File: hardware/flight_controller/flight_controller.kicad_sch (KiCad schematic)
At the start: 15 parts, among them U1 BQ25883RGER

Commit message: Finsihed battery charger wiring
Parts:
- added C5: 10uF, symbol Device:C
- added C6: 44uF, symbol Device:C
- added J1: Conn_01x02_Pin, symbol Connector:Conn_01x02_Pin
- added R10: 10K, Resistor_SMD:R_0201_0603Metric, symbol Device:R
- added R11: 30.1K, Resistor_SMD:R_0201_0603Metric, symbol Device:R
- added R8: 383, Resistor_SMD:R_0201_0603Metric, symbol Device:R
- added R9: 5.23K, Resistor_SMD:R_0201_0603Metric, symbol Device:R
- C4: value 4.7uF -> 10uF
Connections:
- net BQ_PG: now also R7.2; no longer R7.1
- net GND: now also C5.1, C6.1, J1.2 (Pin_2), R10.1, R11.1, R8.2
- net VBUS: now also U1.15 (SYS), U1.16 (SYS), C6.2
- net VREGN: now reaches C4.1, U1.11 (REGN)
- net VREGN: now also R9.2
- net BAT+: now reaches U1.13 (BAT)
- net BAT+: now also U1.14 (BAT), C5.2, J1.1 (Pin_1)
- net BQ_CE: now reaches U1.3 (~{CE})
- net at U1.7 (TS): now also R10.2, R11.2, R9.1
- net at U1.8 (ILIM): now also R8.1
- net +3.3V: now reaches R3.1, R4.2, R5.2, R6.2
- net +3.3V: now also R7.1; no longer R7.2
- net BQ_SCL renamed I2C_SCL
- net BQ_SDA renamed I2C_SDA
- no-connect marks 4 -> 5

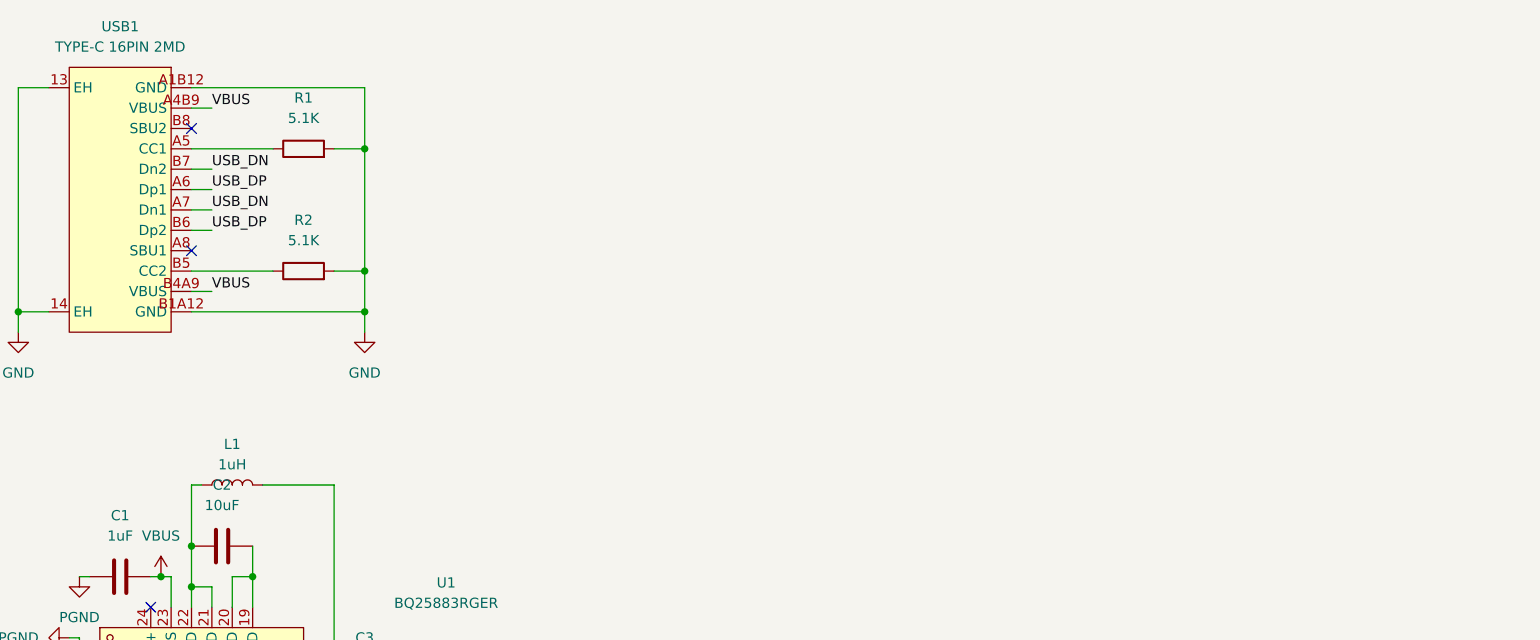
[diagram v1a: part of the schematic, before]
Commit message: Finished wiring for battery regulator
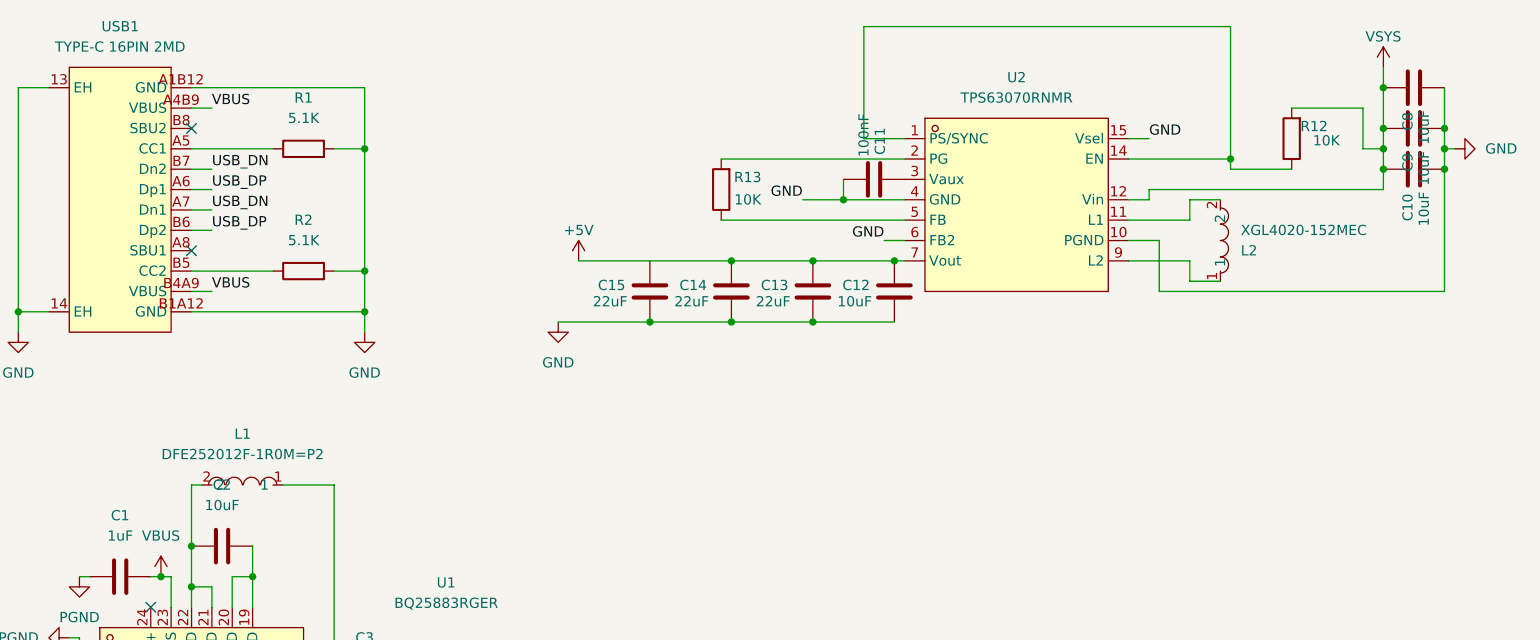
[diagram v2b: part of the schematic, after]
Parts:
- removed L1: 1uH, symbol Device:L
- added C10, C8, C9: 10uF, Capacitor_SMD:C_0805_2012Metric, symbol Device:C
- added C11: 100nF, Capacitor_SMD:C_0805_2012Metric, symbol Device:C
- added C12: 10uF, Capacitor_SMD:C_0603_1608Metric, symbol Device:C
- added C13, C14, C15: 22uF, Capacitor_SMD:C_0805_2012Metric, symbol Device:C
- added L1: DFE252012F-1R0M=P2, easyeda2kicad:L2520, symbol easyeda2kicad:DFE252012F-1R0M=P2
- added L2: XGL4020-152MEC, easyeda2kicad:IND-SMD_L4.0-W4.0_XEL4020, symbol easyeda2kicad:XGL4020-152MEC
- added R12, R13: 10K, Resistor_SMD:R_0201_0603Metric, symbol Device:R
- added U2: TPS63070RNMR, easyeda2kicad:VQFN-15_L3.0-W2.5-P0.50-BL, symbol easyeda2kicad:TPS63070RNMR
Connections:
- net GND: now also C10.2, C11.2, C12.2, C13.2, C14.2, C15.2, C8.2, C9.2, U2.10 (PGND), U2.15 (Vsel), U2.4 (GND), U2.6 (FB2)
- net at C3.1, U1.17 (SW), U1.18 (SW): now also L1.1
- net at C2.1, U1.21 (PMID), U1.22 (PMID): now also L1.2
- new net: R13.1, U2.5 (FB)
- new net: R13.2, U2.2 (PG)
- new net: L2.1, U2.9 (L2)
- new net: L2.2, U2.11 (L1)
- new net: R12.1, U2.1 (PS/SYNC), U2.14 (EN)
- new net: C11.1, U2.3 (Vaux)
- new net +5V: C12.1, C13.1, C14.1, U2.7 (Vout)
- new net VSYS: C10.1, C8.1, C9.1, R12.2, U2.12 (Vin)

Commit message: Wired 3.3V buck, barometer, and IMU
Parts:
- added C15: 2.2uF, Capacitor_SMD:C_0603_1608Metric, symbol Device:C
- added C16, C19, C20, C21, C22: 100nF, Capacitor_SMD:C_0201_0603Metric, symbol Device:C
- added C17, C18: 22uF, Capacitor_SMD:C_0402_1005Metric, symbol Device:C
- added L3: YHNR3015-5R6M, easyeda2kicad:IND-SMD_L3.0-W3.0, symbol easyeda2kicad:YHNR3015-5R6M
- added R14: 100K, Resistor_SMD:R_0402_1005Metric, symbol Device:R
- added R15: 22.1K, Resistor_SMD:R_0402_1005Metric, symbol Device:R
- added U3: LMR51430XDDCR, easyeda2kicad:SOT-23-6_L2.9-W1.6-P0.95-LS2.8-BL, symbol easyeda2kicad:LMR51430XDDCR
- added U4: BMP581, easyeda2kicad:LGA-10_L2.0-W2.0-P0.50-TL_BMP581, symbol easyeda2kicad:BMP581
- added U5: ICM-45686, easyeda2kicad:LGA-14_L3.0-W2.5-P0.50-TL, symbol easyeda2kicad:ICM-45686
- renumbered C11 to C10, C12 to C11, C13 to C12, C14 to C13, C15 to C14, C8 to C7, C9 to C8, C10 to C9
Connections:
- net +3.3V: now also C17.1, C18.1, C19.1, C20.1, C21.1, C22.1, L3.2, R14.2, U4.1 (VDDIO), U4.10 (VDD), U4.6 (CSB), U5.5 (VDDIO), U5.8 (VDD)
- net GND: now also C15.2, C17.2, C18.2, C19.2, C20.2, C21.2, C22.2, R15.1, U3.1 (GND), U4.3 (VSS), U4.5 (SDO), U4.8 (VSS), U4.9 (VSS), U5.6 (GND)
- net I2C_SCL: now also U4.2 (SCK)
- net I2C_SDA: now also U4.4 (SDI)
- net VSYS: now also C15.1, U3.3 (VIN), U3.5 (EN)
- new net: C16.2, L3.1, U3.2 (SW)
- new net: R14.1, R15.2, U3.4 (FB)
- new net: C16.1, U3.6 (CB)
- new net BMP_INT: U4.7 (INT)
- new net ICM_CS: U5.12 (AP_CS)
- new net ICM_INT1: U5.4 (INT1/INT)
- new net ICM_INT2: U5.9 (INT2/FSYNC/CLKIN)
- new net ICM_SCK: U5.13 (AP_SCL/AP_SCLK)
- new net ICM_SDI: U5.14 (AP_SDA/AP_SDIO/AP_SDI)
- new net ICM_SDO: U5.1 (AP_SDO/AP_AD0)
- no-connect marks 5 -> 10

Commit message: GPS, MicroSD, and Magnetometer
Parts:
- added C23: 220nF, Capacitor_SMD:C_0201_0603Metric, symbol Device:C
- added C24, C26: 100nF, Capacitor_SMD:C_0201_0603Metric, symbol Device:C
- added C25: 10uF, Capacitor_SMD:C_0201_0603Metric, symbol Device:C
- added C27: 47pF, Capacitor_SMD:C_0201_0603Metric, symbol Device:C
- added Card1: TF-01A, easyeda2kicad:TF-SMD_TF-01A, symbol easyeda2kicad:TF-01A
- added JP1: U.FL-R-SMT-1, easyeda2kicad:ANT-SMD_UFL-R-SMT-1-10, symbol easyeda2kicad:U.FL-R-SMT-1
- added L4: LQG15HN27NJ02D, easyeda2kicad:L0402, symbol easyeda2kicad:LQG15HN27NJ02D
- added R16, R17, R18, R19, R20, R21: 10K, Resistor_SMD:R_0201_0603Metric, symbol Device:R
- added R22: 120, Resistor_SMD:R_0201_0603Metric, symbol Device:R
- added R23: 10, Resistor_SMD:R_0201_0603Metric, symbol Device:R
- added TP2: TestPoint, symbol Connector:TestPoint
- added U6: LIS2MDLTR, easyeda2kicad:VLGA-12_L2.0-W2.0-P0.50-BL, symbol easyeda2kicad:LIS2MDLTR
- added U7: NEO-M8U-06B, easyeda2kicad:GPSM-SMD_24P-L16.0-W12.2-P1.10-TL, symbol easyeda2kicad:NEO-M8U-06B
- added U8: YLED0603G, easyeda2kicad:LED0603-FD, symbol easyeda2kicad:YLED0603G
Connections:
- net +3.3V: now also C24.1, C25.1, C26.1, Card1.4 (VDD), R16.2, R17.2, R18.2, R19.2, R20.2, R21.2, U6.10 (Vdd_IO), U6.9 (Vdd), U7.22 (V_BCKP), U7.23 (VCC)
- net +5V: now also C14.1
- net GND: now also C2.2, U1.19 (GND), U1.20 (GND), C23.2, C24.2, C25.2, C26.2, C27.2, Card1.10 (GND), Card1.11 (GND), Card1.12 (GND), Card1.13 (GND), Card1.6 (VSS), JP1.1 (GND), JP1.3 (GND), U6.6 (GND), U6.8 (GND), U7.10 (GND), U7.12 (GND), U7.13 (GND), U7.2 (D_SEL), U7.24 (GND), U7.7 (VDD_USB), U8.2 (-)
- new net: C23.1, U6.5 (C1)
- new net: R22.1, U8.1 (+)
- new net: R22.2, U7.3 (TIMEPULSE)
- new net: C27.1, L4.2, R23.1
- new net: R23.2, U7.9 (VCC_RF)
- new net: TP2.1, U7.1 (SAFEBOOT_N)
- new net GPS_CS: U7.18 (SDA/SPICS_N)
- new net GPS_EXTINT: U7.4 (EXTINT)
- new net GPS_RESETN: U7.8 (RESET_N)
- new net GPS_SCK: U7.19 (SCL/SPICLK)
- new net GPS_SDI: U7.21 (RXD/SPIMOSI)
- new net GPS_SDO: U7.20 (TXD/SPIMISO)
- new net MAG_CS: U6.3 (CS)
- new net MAG_SCK: U6.1 (SCL/SPC)
- new net MAG_SDI: U6.4 (SDA/SDI/SDO)
- new net MAG_SDO: U6.7 (INT/DRDY/SDO)
- new net RF_IN: JP1.2 (SIN), L4.1, U7.11 (RF_IN)
- new net SD_CD: Card1.9 (CD)
- new net SD_CLK: Card1.5 (CLK(SCLK)), R21.1
- new net SD_CMD: Card1.3 (CMD(DI)), R20.1
- new net SD_DAT0: Card1.7 (DAT0(D0)), R16.1
- new net SD_DAT1: Card1.8 (DAT1(RSV)), R17.1
- new net SD_DAT2: Card1.1 (DAT2(RSV)), R18.1
- new net SD_DAT3: Card1.2 (CDDAT3(CS)), R19.1
- no-connect marks 10 -> 19
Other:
- moved on the sheet: C1, C10, C11, C12, C13, C14, C15, C16, C17, C18, C19, C2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

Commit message: nothing
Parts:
- added C28: 100nF, Capacitor_SMD:C_0201_0603Metric, symbol Device:C
- added U9: Ai-Thinker-Ra-02, RF_Module:Ai-Thinker-Ra-01-LoRa, symbol RF_Module:Ai-Thinker-Ra-02
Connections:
- net +3.3V: now also C28.1, U9.3 (VDD)
- net GND: now also C28.2, U9.1 (GND), U9.16 (GND), U9.2 (GND), U9.9 (GND)
- net VBUS: no longer C6.2, U1.15 (SYS), U1.16 (SYS)
- net VSYS: now also C6.2, U1.15 (SYS), U1.16 (SYS)
- net GPS_RESETN renamed GPS_RESET
- new net RF_CS: U9.15 (~{NSS})
- new net RF_DIO0: U9.5 (DIO0)
- new net RF_DIO1: U9.6 (DIO1)
- new net RF_DIO2: U9.7 (DIO2)
- new net RF_DIO3: U9.8 (DIO3)
- new net RF_DIO4: U9.10 (DIO4)
- new net RF_DIO5: U9.11 (DIO5)
- new net RF_RESET: U9.4 (~{RESET})
- new net RF_SCK: U9.12 (SCK)
- new net RF_SDI: U9.14 (MOSI)
- new net RF_SDO: U9.13 (MISO)

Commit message: Finsihed schematic
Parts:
- removed C1: 1uF, symbol Device:C
- removed C2, C4, C5: 10uF, symbol Device:C
- removed C3: 47nF, symbol Device:C
- removed C6: 44uF, symbol Device:C
- removed D1: LED, symbol Device:LED
- removed J1: Conn_01x02_Pin, symbol Connector:Conn_01x02_Pin
- removed L1: DFE252012F-1R0M=P2, easyeda2kicad:L2520, symbol easyeda2kicad:DFE252012F-1R0M=P2
- removed R10: 10K, Resistor_SMD:R_0201_0603Metric, symbol Device:R
- removed R11: 30.1K, Resistor_SMD:R_0201_0603Metric, symbol Device:R
- removed R3, R4, R5, R6, R7: 10K, symbol Device:R
- removed R8: 383, Resistor_SMD:R_0201_0603Metric, symbol Device:R
- removed R9: 5.23K, Resistor_SMD:R_0201_0603Metric, symbol Device:R
- removed U1: BQ25883RGER, easyeda2kicad:VFQFPN-24_L4.0-W4.0-P0.50-BL-EP2.8, symbol easyeda2kicad:BQ25883RGER
- added C29, C30, C31, C32, C33, C42, C45: 100nF, Capacitor_SMD:C_0201_0603Metric, symbol Device:C
- added C34, C35, C36, C46, C47: 1uF, Capacitor_SMD:C_0402_1005Metric, symbol Device:C
- added C37: 10uF, Capacitor_SMD:C_0402_1005Metric, symbol Device:C
- added C38, C39: 20pF, Capacitor_SMD:C_0201_0603Metric, symbol Device:C
- added C40, C41: 6.8pF, Capacitor_SMD:C_0201_0603Metric, symbol Device:C
- added C43, C44: 2.2uF, Capacitor_SMD:C_0603_1608Metric, symbol Device:C
- added C48, C50: 10uF, Capacitor_SMD:C_0603_1608Metric, symbol Device:C
- added C49: 4.7uF, Capacitor_SMD:C_0402_1005Metric, symbol Device:C
- added C51: 47nF, Capacitor_SMD:C_0201_0603Metric, symbol Device:C
- added D2: LED, easyeda2kicad:LED0603-FD, symbol Device:LED
- added J2: Camera_Connector, symbol Connector_Generic:Conn_01x06
- added J3: ESC_Connector, symbol Connector_Generic:Conn_01x08
- added J4: ESC_Battery_Solder_Pads, Library:ESC_BATTERY_SOLDER_PADS, symbol Connector_Generic:Conn_01x02
- added J5: Battery_Connector, Connector_JST:JST_XH_B3B-XH-A_1x03_P2.50mm_Vertical, symbol Connector_Generic:Conn_01x03
- added JP2: U.FL-R-SMT-1, easyeda2kicad:ANT-SMD_UFL-R-SMT-1-10, symbol easyeda2kicad:U.FL-R-SMT-1
- added L5: FCM1608KF-601T03, easyeda2kicad:L0603, symbol easyeda2kicad:FCM1608KF-601T03
- added L6: DFE252012F-1R0M=P2, easyeda2kicad:L2520, symbol easyeda2kicad:DFE252012F-1R0M=P2
- added R24, R35: 10K, Resistor_SMD:R_0201_0603Metric, symbol Device:R
- added R25, R26, R27, R28, R29: 10K, symbol Device:R
- added R30: 383, Resistor_SMD:R_0201_0603Metric, symbol Device:R
- added R31: 300, Resistor_SMD:R_0201_0603Metric, symbol Device:R
- added R32: 15, Resistor_SMD:R_1206_3216Metric, symbol Device:R
- added R33: 5.23K, Resistor_SMD:R_0201_0603Metric, symbol Device:R
- added R34: 30.1K, Resistor_SMD:R_0201_0603Metric, symbol Device:R
- added SW1, SW2: TS-1088-AR02016, easyeda2kicad:SW-SMD_L3.9-W3.0-P4.45, symbol easyeda2kicad:TS-1088-AR02016
- added U10: STM32H743VIT6_C114409, easyeda2kicad:LQFP-100_L14.0-W14.0-P0.50-LS16.0-BL, symbol easyeda2kicad:STM32H743VIT6_C114409
- added U11: ANT1204F002R0433A, footprints:CHIP_R0433A_YAG, symbol PassiveAntennaSMDForLoRa:ANT1204F002R0433A
- added U12: BQ25887RGER, easyeda2kicad:WQFN-24_EP_4.0X4.0X0.5P, symbol easyeda2kicad:BQ25887RGER
- added X1: X322525MOB4SI, easyeda2kicad:CRYSTAL-SMD_4P-L3.2-W2.5-BL, symbol easyeda2kicad:X322525MOB4SI
- added X2: Q13FC1350000400, easyeda2kicad:FC-135R_L3.2-W1.5, symbol easyeda2kicad:Q13FC1350000400
- C10: footprint Capacitor_SMD:C_0805_2012Metric -> Capacitor_SMD:C_0201_0603Metric
- C25: footprint Capacitor_SMD:C_0201_0603Metric -> Capacitor_SMD:C_0402_1005Metric
- C9: footprint Capacitor_SMD:C_0805_2012Metric -> Capacitor_SMD:C_0603_1608Metric
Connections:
- net ICM_SCK is gone; now on net SPI_SCK: U5.13 (AP_SCL/AP_SCLK)
- net ICM_SDI is gone; now on net SPI_SDI: U5.14 (AP_SDA/AP_SDIO/AP_SDI)
- net ICM_SDO is gone; now on net SPI_SDO: U5.1 (AP_SDO/AP_AD0)
- net MAG_SCK is gone; now on net SPI_SCK: U6.1 (SCL/SPC)
- net MAG_SDI is gone; now on net SPI_SDI: U6.4 (SDA/SDI/SDO)
- net MAG_SDO is gone; now on net SPI_SDO: U6.7 (INT/DRDY/SDO)
- net RF_SCK is gone; now on net SPI_SCK: U9.12 (SCK)
- net RF_SDI is gone; now on net SPI_SDI: U9.14 (MOSI)
- net RF_SDO is gone; now on net SPI_SDO: U9.13 (MISO)
- net +3.3V: now also C29.1, C30.1, C31.1, C32.1, C33.1, C34.1, C35.1, C36.1, C37.1, C45.1, C46.1, D2.1 (K), L5.2, R25.2, R26.2, R28.2, R29.2, SW2.1, U10.100 (VDD), U10.11 (VDD), U10.27 (VDD), U10.50 (VDD), U10.6 (VBAT), U10.75 (VDD)
- net +5V: now also R13.1, U2.5 (FB), J2.1 (Pin_1)
- net BMP_INT: now also U10.59 (PD12)
- net BQ_CE: now also U10.58 (PD11), U12.3 (CD)
- net BQ_INT: now also R28.1, U10.60 (PD13), U12.6 (~{INT})
- net BQ_PG: now also R29.1, U12.1 (~{PG})
- net GND: now also C29.2, C30.2, C31.2, C32.2, C33.2, C34.2, C35.2, C36.2, C37.2, C38.2, C39.2, C40.2, C41.2, C42.1, C43.2, C44.2, C45.2, C46.2, C47.1, C48.1, C49.2, C50.1, J2.2 (Pin_2), J2.5 (Pin_5), J3.2 (Pin_2), J4.2 (Pin_2), J5.1 (Pin_1), JP2.1 (GND), JP2.3 (GND), R24.1, R30.2, R34.1, R35.1, SW1.1, U10.10 (VSS), U10.19 (VSSA), U10.26 (VSS), U10.49 (VSS), U10.74 (VSS), U10.99 (VSS), U12.19 (GND), U12.20 (GND), U12.24 (PSEL), U12.25 (EP), X1.2 (GND), X1.4 (GND)
- net GPS_CS: now also U10.35 (PB1)
- net GPS_EXTINT: now also U10.25 (PA3)
- net GPS_RESET: now also U10.24 (PA2)
- net I2C_SCL: now also R26.1, U10.92 (PB6), U12.5 (SCL)
- net I2C_SDA: now also R25.1, U10.93 (PB7), U12.4 (SDA)
- net ICM_CS: now also U10.28 (PA4)
- net ICM_INT1: now also U10.32 (PC4)
- net ICM_INT2: now also U10.33 (PC5)
- net MAG_CS: now also U10.34 (PB0)
- net RF_CS: now also U10.36 (PB2)
- net RF_DIO0: now also U10.23 (PA1)
- net RF_DIO1: now also U10.1 (PE2)
- net RF_RESET: now also U10.22 (PA0)
- net SD_CD: now also U10.81 (PD0)
- net SD_CLK: now also U10.80 (PC12)
- net SD_CMD: now also U10.83 (PD2)
- net SD_DAT0: now also U10.65 (PC8)
- net SD_DAT1: now also U10.66 (PC9)
- net SD_DAT2: now also U10.78 (PC10)
- net SD_DAT3: now also U10.79 (PC11)
- net USB_DN: now also U10.70 (PA11)
- net VBUS: now also C47.2, U12.23 (VBUS)
- net VREGN: now also C48.2, R33.2, U12.11 (REGN)
- net at USB1.A6 (Dp1), USB1.B6 (Dp2): now also U10.71 (PA12)
- net GPS_SCK renamed SPI_SCK
- net SPI_SCK: now also U10.29 (PA5)
- net GPS_SDI renamed SPI_SDI
- net SPI_SDI: now also U10.31 (PA7)
- net GPS_SDO renamed SPI_SDO
- net SPI_SDO: now also U10.30 (PA6)
- net RF_DIO2: no longer names the net of U9.7 (DIO2)
- net RF_DIO3: no longer names the net of U9.8 (DIO3)
- net RF_DIO4: no longer names the net of U9.10 (DIO4)
- net RF_DIO5: no longer names the net of U9.11 (DIO5)
- new net: R27.1, U12.2 (STAT)
- new net: D2.2 (A), R27.2
- new net: C43.1, U10.73 (VCAP)
- new net: R32.1, U12.10 (CBSET)
- new net: C51.1, U12.12 (BTST)
- new net: J5.3 (Pin_3), U12.13 (BAT), U12.14 (BAT)
- new net: C49.1, U12.15 (SNS), U12.16 (SNS)
- new net: C51.2, L6.1, U12.17 (SW), U12.18 (SW)
- new net: C50.2, L6.2, U12.21 (PMID), U12.22 (PMID)
- new net: R33.1, R34.2, R35.2, U12.7 (TS)
- new net: R30.1, U12.8 (ILIM)
- new net: R31.1, U12.9 (MID)
- new net: L5.1, U10.20 (VREF+), U10.21 (VDDA)
- new net: C44.1, U10.48 (VCAP)
- new net: J5.2 (Pin_2), R31.2, R32.2
- new net ANT_IN: JP2.2 (SIN), U11.1
- new net BAT_POSITIVE: J4.1 (Pin_1)
- new net BOOT: R24.2, SW2.2, U10.94 (BOOT0)
- new net CAM_RX: J2.3 (Pin_3), U10.98 (PE1)
- new net CAM_TX: J2.4 (Pin_4), U10.97 (PE0)
- new net ESC_BAT: J3.1 (Pin_1), U10.16 (PC1)
- new net ESC_M1: J3.3 (Pin_3), U10.39 (PE9)
- new net ESC_M2: J3.4 (Pin_4), U10.41 (PE11)
- new net ESC_M3: J3.5 (Pin_5), U10.43 (PE13)
- new net ESC_M4: J3.6 (Pin_6), U10.44 (PE14)
- new net HSE_IN: C38.1, U10.12 (PH0-OSC_IN), X1.1 (OSC1)
- new net HSE_OUT: C39.1, U10.13 (PH1-OSC_OUT), X1.3 (OSC2)
- new net LSE_IN: C40.1, U10.8 (PC14-OSC32_IN), X2.1
- new net LSE_OUT: C41.1, U10.9 (PC15-OSC32_OUT), X2.2
- new net RESET: C42.2, SW1.2, U10.14 (NRST)
- no-connect marks 19 -> 66
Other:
- note added: "3.3V Buck"
- note added: "5V Buck Boost"
- note added: "Antenna"
- note added: "Barometer"
- note added: "Battery Charger"
- note added: "Connectors"
- note added: "Crystals"
- note added: "GPS"
- note added: "IMU"
- note added: "LoRa Transmitter"
- note added: "Magnetometer"
- note added: "MicroSD"
- note added: "Microcontroller"
- note added: "Switches"
- note added: "USB"
- title: (none) -> Express Flight Controller
- moved on the sheet: C10, C11, C12, C13, C14, C15, C16, C17, C18, C19, C20, C21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

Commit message: PCB Deisgn Part 1
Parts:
- removed J4: ESC_Battery_Solder_Pads, Library:ESC_BATTERY_SOLDER_PADS, symbol Connector_Generic:Conn_01x02
- added C52: 10uF, Capacitor_SMD:C_0603_1608Metric, symbol Device:C
- C43, C44: footprint Capacitor_SMD:C_0603_1608Metric -> Capacitor_SMD:C_0201_0603Metric
- C48, C50: footprint Capacitor_SMD:C_0603_1608Metric -> Capacitor_SMD:C_0402_1005Metric
- D2: footprint easyeda2kicad:LED0603-FD -> LED_SMD:LED_0402_1005Metric
- J2: footprint (none) -> Connector_JST:JST_SH_BM06B-SRSS-TB_1x06-1MP_P1.00mm_Vertical
- J3: footprint (none) -> Connector_JST:JST_SH_BM08B-SRSS-TB_1x08-1MP_P1.00mm_Vertical
- R1, R2, R25, R26, R27, R28, R29: footprint (none) -> Resistor_SMD:R_0201_0603Metric
- TP2: footprint (none) -> TestPoint:TestPoint_Pad_1.0x1.0mm
- U12: footprint easyeda2kicad:WQFN-24_EP_4.0X4.0X0.5P -> easyeda2kicad:VFQFPN-24_L4.0-W4.0-P0.50-BL-EP2.8
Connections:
- net GND: now also C52.2
- net at J5.3 (Pin_3), U12.13 (BAT), U12.14 (BAT): now also C52.1
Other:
- moved on the sheet: J2, J3
